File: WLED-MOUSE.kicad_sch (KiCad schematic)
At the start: 15 parts, among them J1 FTDI-header, J2 Power-in, J3 Conn_01x03_Female, J4 Pixel-strip, J5 Conn_01x03_Female, J6 Pixel-strip, J7 Pixel-strip, J8 Pixel-strip, U1 ESP32-WROOM-32D, U2 ESP32-WROOM-32D, U3 SN74LV4T125

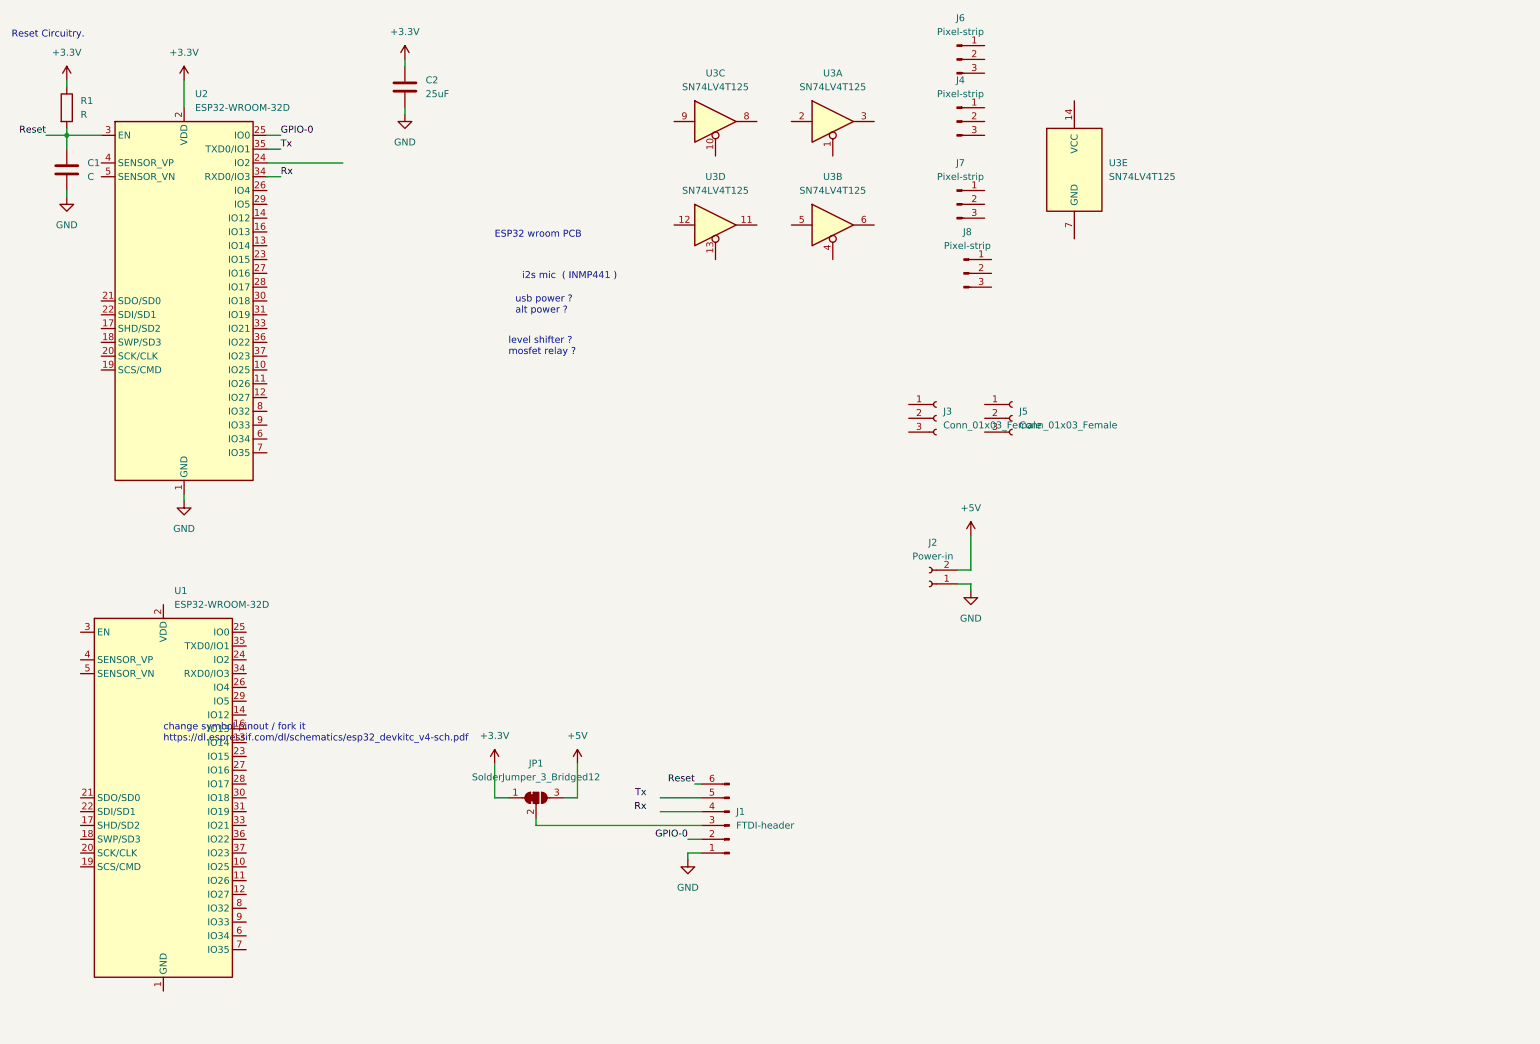
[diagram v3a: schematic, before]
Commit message: wired up the schimatic for the level shifters.
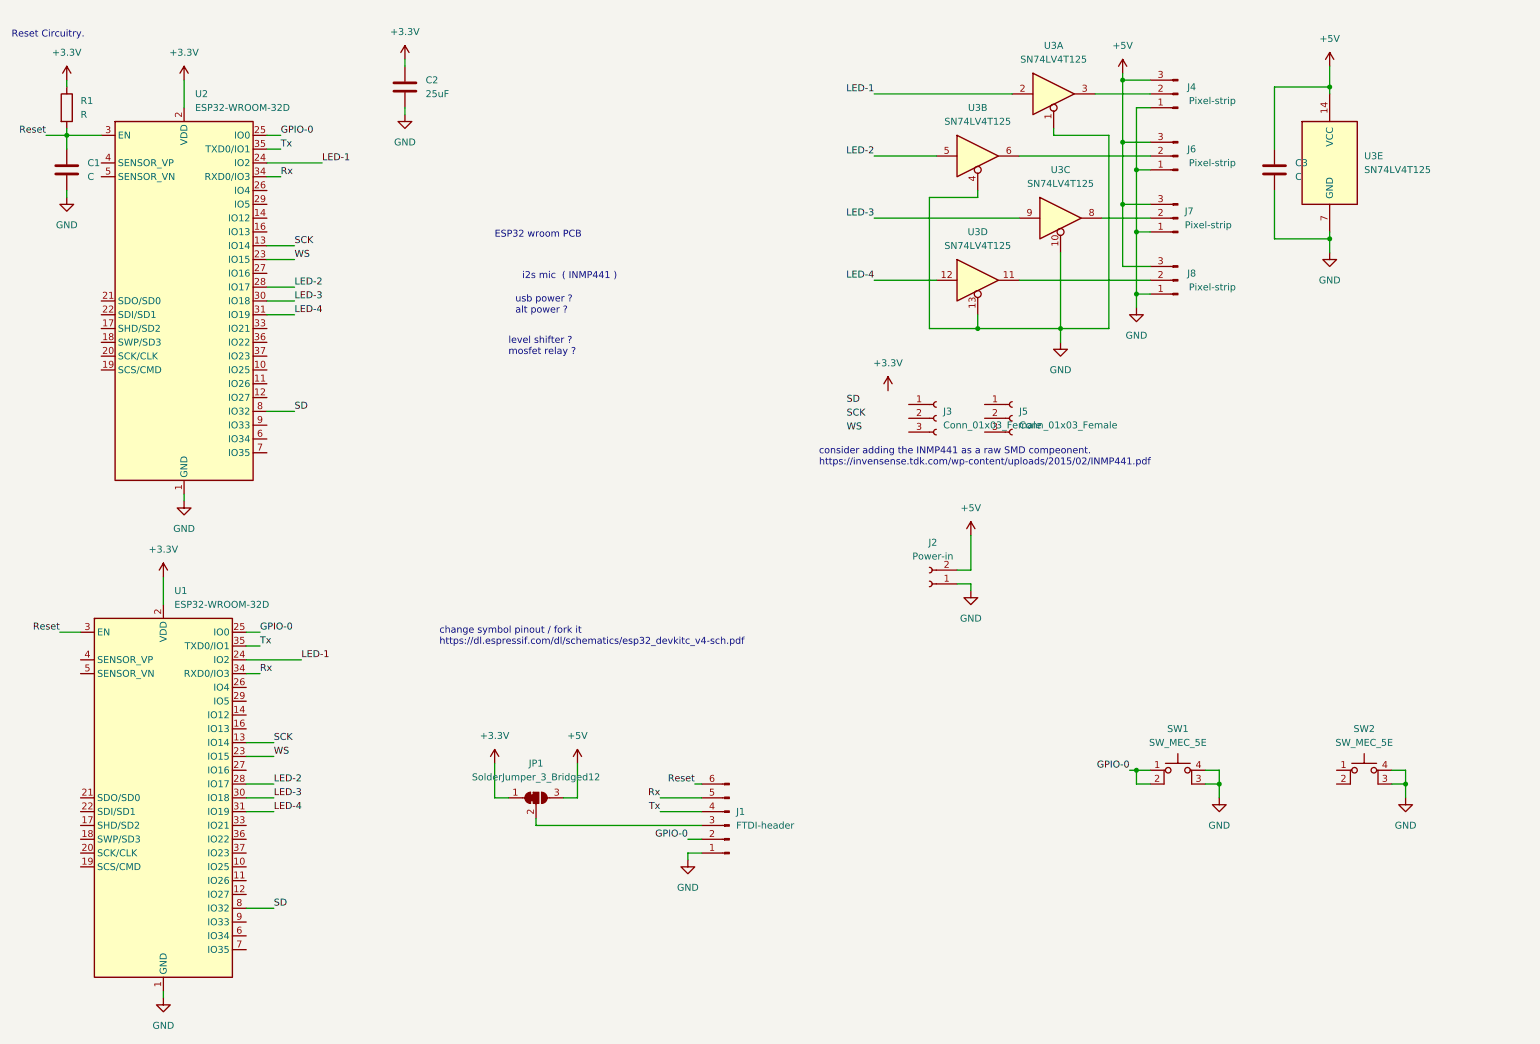
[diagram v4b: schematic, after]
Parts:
- added C3: C, Capacitor_SMD:C_0805_2012Metric, symbol Device:C
- added SW1, SW2: SW_MEC_5E, Button_Switch_THT:SW_PUSH_6mm_H5mm, symbol Switch:SW_MEC_5E
- J5: footprint (none) -> Connector_PinSocket_2.54mm:PinSocket_1x03_P2.54mm_Vertical
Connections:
- net +3.3V: now also U1.2 (VDD)
- net +5V: now also J4.3 (Pin_3), J6.3 (Pin_3), J7.3 (Pin_3), J8.3 (Pin_3), U3.14 (VCC), C3.1
- net GND: now also J4.1 (Pin_1), J6.1 (Pin_1), J7.1 (Pin_1), J8.1 (Pin_1), U1.1 (GND), U1.15 (GND), U1.38 (GND), U1.39 (GND), U3.1, U3.10, U3.13, U3.4, U3.7 (GND), C3.2, SW1.3 (K), SW1.4 (A), SW2.3 (K), SW2.4 (A)
- net GPIO-0: now also U1.25 (IO0), SW1.1, SW1.2
- net Reset: now also U1.3 (EN)
- net Rx: now also J1.5 (Pin_5), U1.34 (RXD0/IO3)
- net Tx: now also J1.4 (Pin_4), U1.35 (TXD0/IO1)
- net at J6.2 (Pin_2): now also U3.6
- net at J7.2 (Pin_2): now also U3.8
- net at U3.11: now also J8.2 (Pin_2)
- net LED-4: now reaches U3.12
- net LED-4: now also U1.31 (IO19), U2.31 (IO19)
- net SCK: now reaches U1.13 (IO14)
- net SCK: now also U2.13 (IO14)
- net WS: now reaches U1.23 (IO15)
- net WS: now also U2.23 (IO15)
- net LED-1: now reaches U1.24 (IO2)
- net LED-1: now also U2.24 (IO2), U3.2
- net LED-2: now reaches U1.28 (IO17)
- net LED-2: now also U2.28 (IO17), U3.5
- net LED-3: now reaches U1.30 (IO18)
- net LED-3: now also U2.30 (IO18), U3.9
- net SD: now reaches U1.8 (IO32)
- net SD: now also U2.8 (IO32)
- net at U3.3: now also J4.2 (Pin_2)
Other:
- note added: "consider adding the INMP441 as a raw SMD compeonent. https://invensense.tdk.com/wp-content/uploads/2015/02/INMP441.pdf"
- moved on the sheet: J4, J6, J7, J8, U3A, U3B, U3C, U3D, U3E

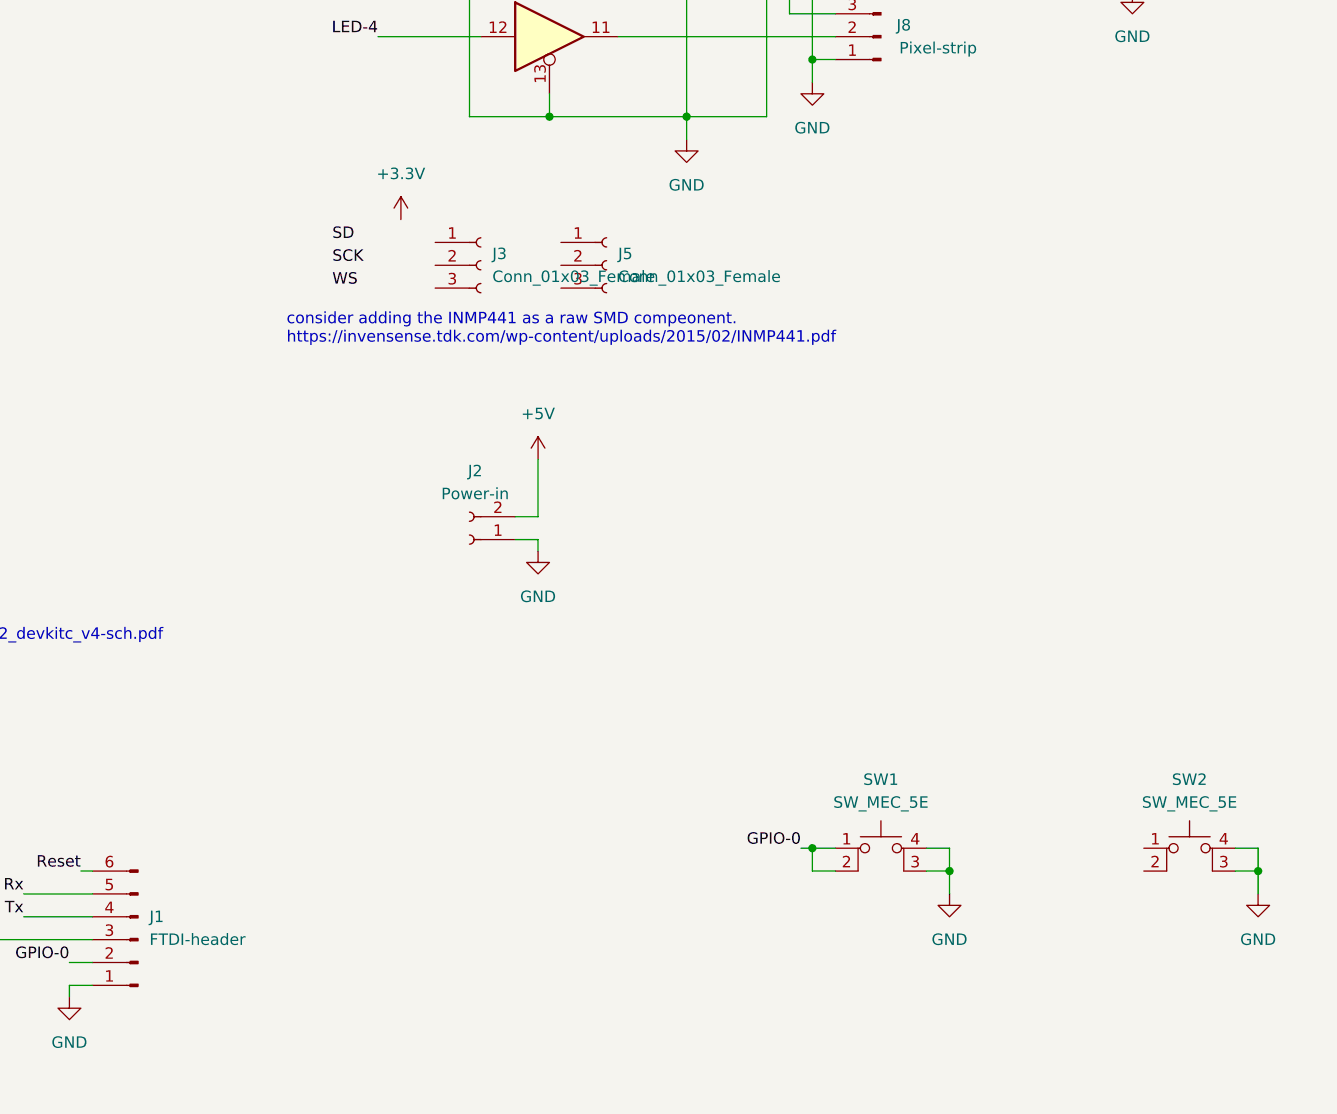
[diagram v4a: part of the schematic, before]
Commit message: added the JLC PCB rules and settings, for eventual prodcution, also tried to add some of the stuff for the mic.
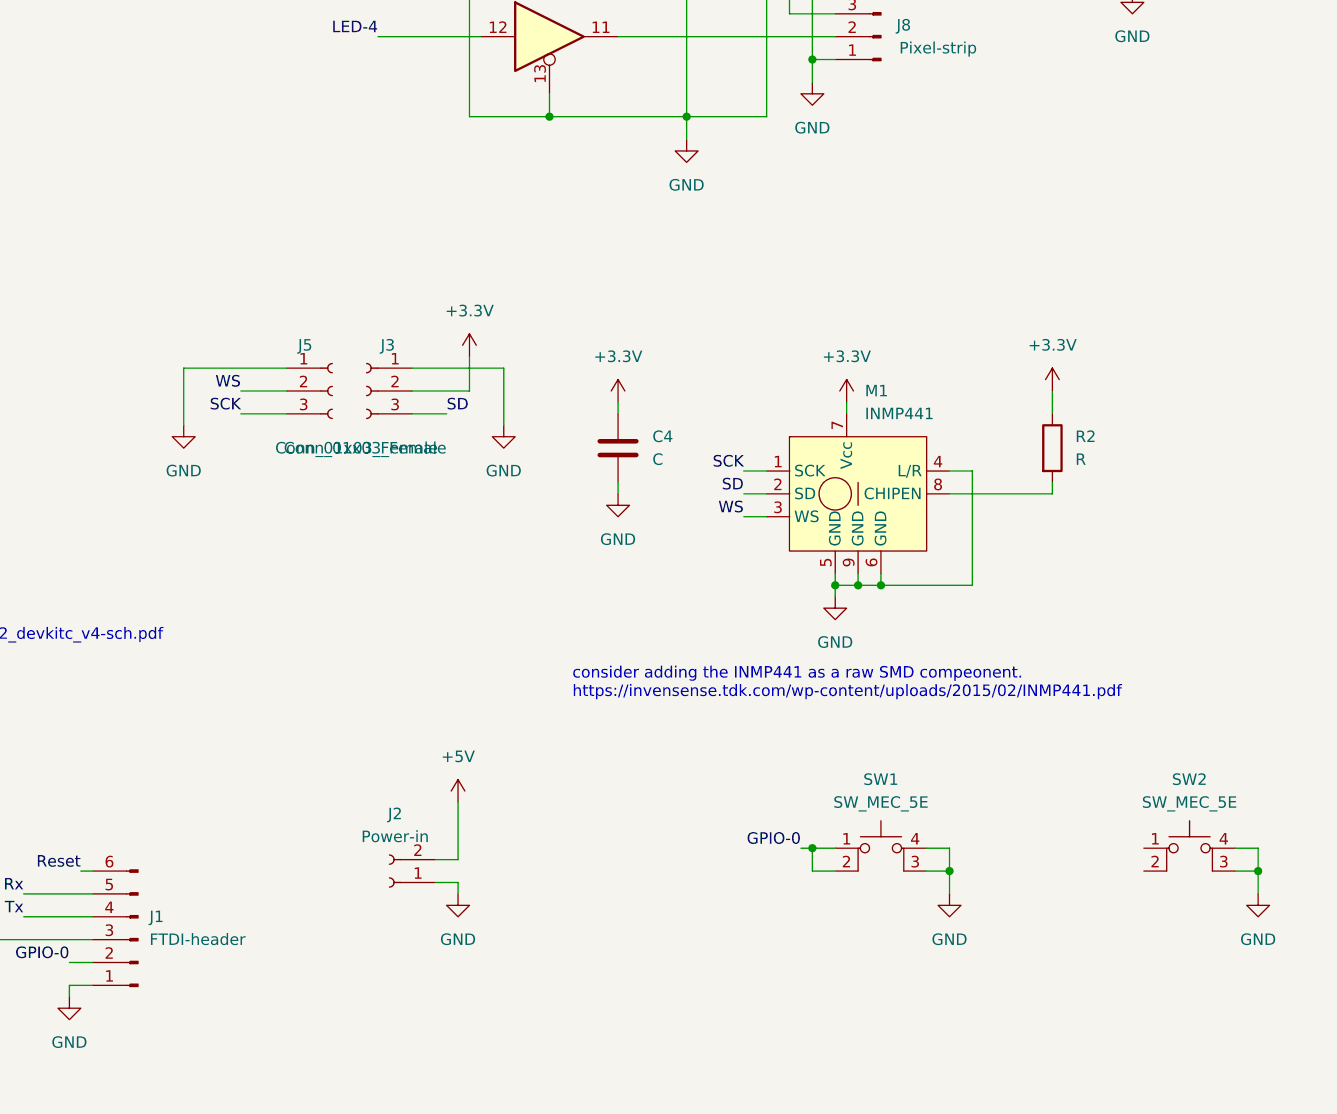
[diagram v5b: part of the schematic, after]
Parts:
- added C4: C, Capacitor_SMD:C_0805_2012Metric, symbol Device:C
- added M1: INMP441, mic:MIC_DMM-4026-B-I2S-R, symbol INMP441:INMP441
- added R2: R, Resistor_SMD:R_0603_1608Metric, symbol Device:R
- J3: footprint (none) -> Connector_PinSocket_2.54mm:PinSocket_1x03_P2.54mm_Vertical
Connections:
- net +3.3V: now also J3.2 (Pin_2), C4.1, M1.7 (Vcc), R2.1
- net GND: now also J3.1 (Pin_1), J5.1 (Pin_1), C4.2, M1.4 (L/R), M1.5 (GND), M1.6 (GND), M1.9 (GND)
- net SCK: now also J5.3 (Pin_3), M1.1 (SCK)
- net SD: now also J3.3 (Pin_3), M1.2 (SD)
- net WS: now also J5.2 (Pin_2), M1.3 (WS)
- new net: M1.8 (CHIPEN), R2.2
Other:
- moved on the sheet: J2, J3, J5

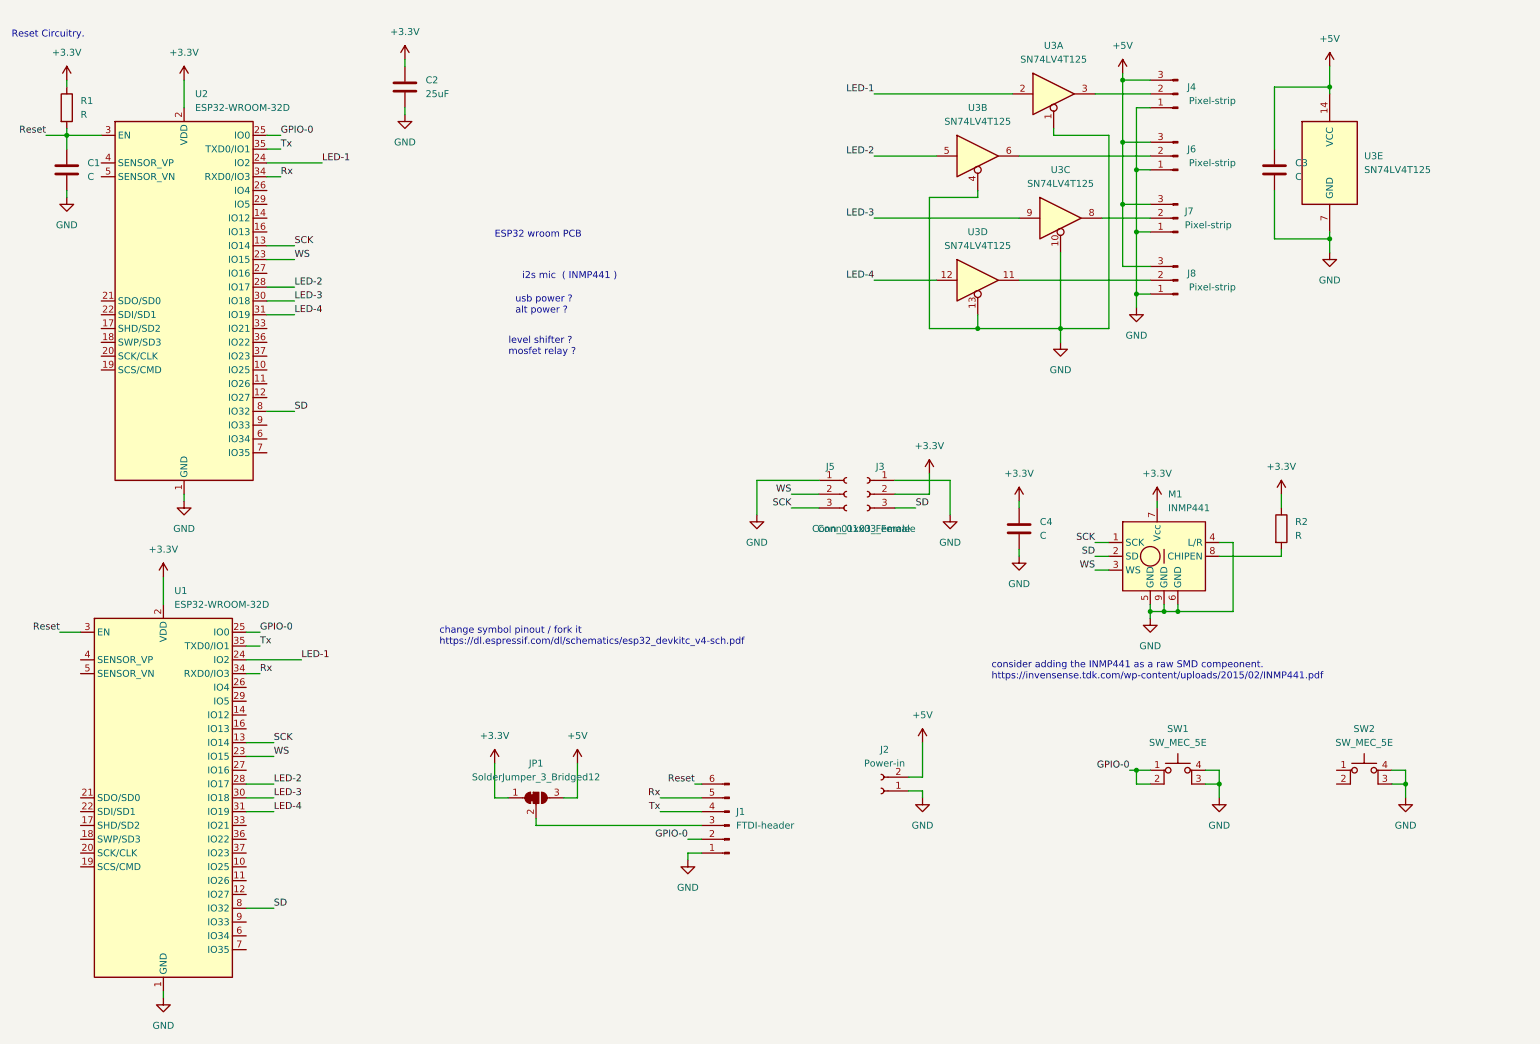
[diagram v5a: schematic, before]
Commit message: added footprint for the thought hole mic board, thing?
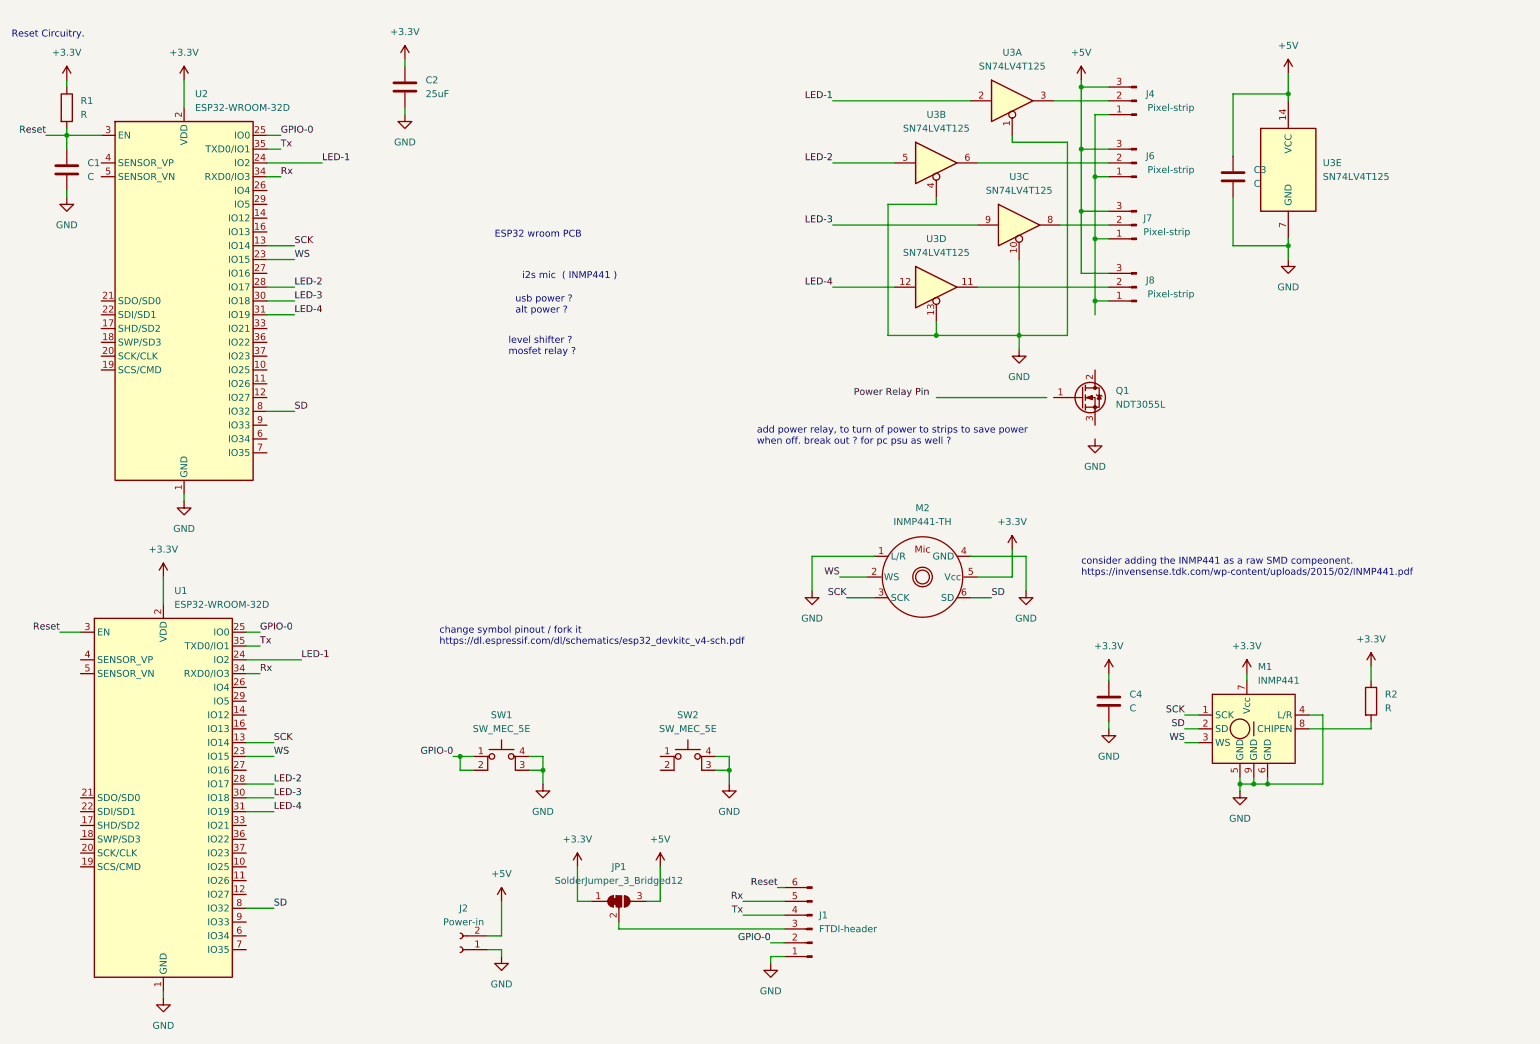
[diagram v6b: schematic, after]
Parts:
- removed J3, J5: Conn_01x03_Female, Connector_PinSocket_2.54mm:PinSocket_1x03_P2.54mm_Vertical, symbol Connector:Conn_01x03_Female
- added M2: INMP441-TH, mic:MIC_DMM-4026-B-I2S-R-TH, symbol INMP441:INMP441-TH
- added Q1: NDT3055L, Package_TO_SOT_SMD:SOT-223-3_TabPin2, symbol Transistor_FET:NDT3055L
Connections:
- net +3.3V: now also M2.5 (Vcc)
- net GND: now also M2.1 (L/R), M2.4 (GND); no longer J4.1 (Pin_1), J6.1 (Pin_1), J7.1 (Pin_1), J8.1 (Pin_1)
- net SCK: now also M2.3 (SCK)
- net SD: now also M2.6 (SD)
- net WS: now also M2.2 (WS)
- new net: J4.1 (Pin_1), J6.1 (Pin_1), J7.1 (Pin_1), J8.1 (Pin_1)
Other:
- note added: "add power relay, to turn of power to strips to save power when off. break out ? for pc psu as well ?"
- moved on the sheet: C3, C4, J1, J2, J4, J6, J7, J8, JP1, M1, R2, SW1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
